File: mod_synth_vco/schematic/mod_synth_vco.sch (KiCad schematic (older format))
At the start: 15 parts

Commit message: Update schematic for vco
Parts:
- added C?: 10nf, symbol Device:C
- added C?: 1nf, symbol Device:C
- added J? (x3): AudioJack2, symbol Connector:AudioJack2
- added R? (x2): 100k, symbol Device:R
- added R? (x2): 10k, symbol Device:R
- added R?: 470k, symbol Device:R
- added RV? (x3): R_POT, symbol Device:R_POT
- added RV?: R_POT_TRIM, symbol Device:R_POT_TRIM
- added U? (x3): TL072, symbol Amplifier_Operational:TL072
- R?: value R -> 24k
- R?: value R -> 1m5
- R?: value R -> 5k6
- R? (x2): value R -> 100k
- R?: value R -> 620
- R?: value R -> 1k8
- R? (x2): value R -> 470
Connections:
- net +12V: now also R?.2, RV?.1, RV?.3, U?.8 (V+)
- net -12V: now also R?.2, U?.4 (V-)
- net GND: now also J?.S, R?.1, R?.2, U?.12 (GND), C?.2, C?.2, J?.S, J?.S, J?.S, R?.2, R?.2, RV?.3, RV?.3
- net at U?.1 (SCALE1): now also R?.1
- net at U?.11 (CAP): now also C?.1
- net at U?.13 (VLFI): now also R?.1, R?.1
- net at U?.14 (VS): now also R?.2
- net at U?.15 (VFCI): now also R?.1, R?.2, R?.2
- net at U?.2 (SCALE2): now also R?.1
- net at U?.3 (VEE): now also R?.1, R?.2, RV?.2, RV?.3
- net at U?.4 (VP): now also R?.1, R?.1, U?.3 (+)
- net at U?.5 (VPWM): now also R?.1
- net at R?.2: now also RV?.1
- net at R?.1: now also J?.T
- net at R?.2: now also C?.1
- net at R?.1: now also RV?.2
- new net: J?.T, RV?.1
- new net: R?.2, RV?.2 (x2)
- new net: J?.T, U?.1, U?.2 (-)
- new net: R?.1, R?.1, U?.5 (+)
- new net: R?.2, U?.6 (-), U?.7
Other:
- moved on the sheet: J?, R?, U?, U?A, U?B, U?C

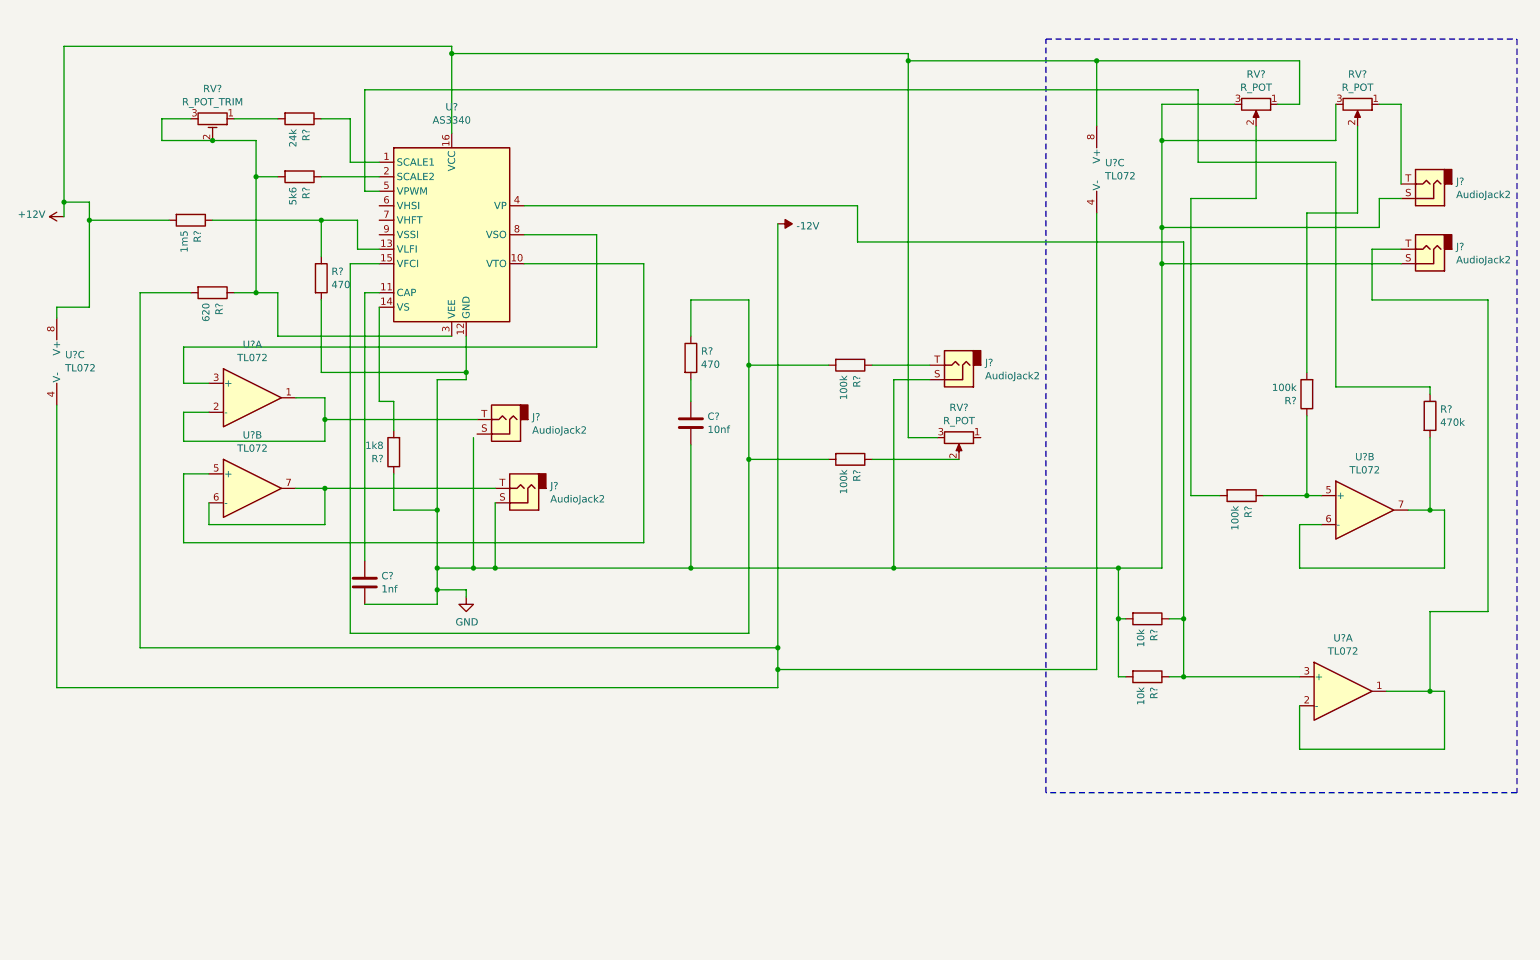
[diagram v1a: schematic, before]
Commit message: Add labels and cleanup square/PWM section
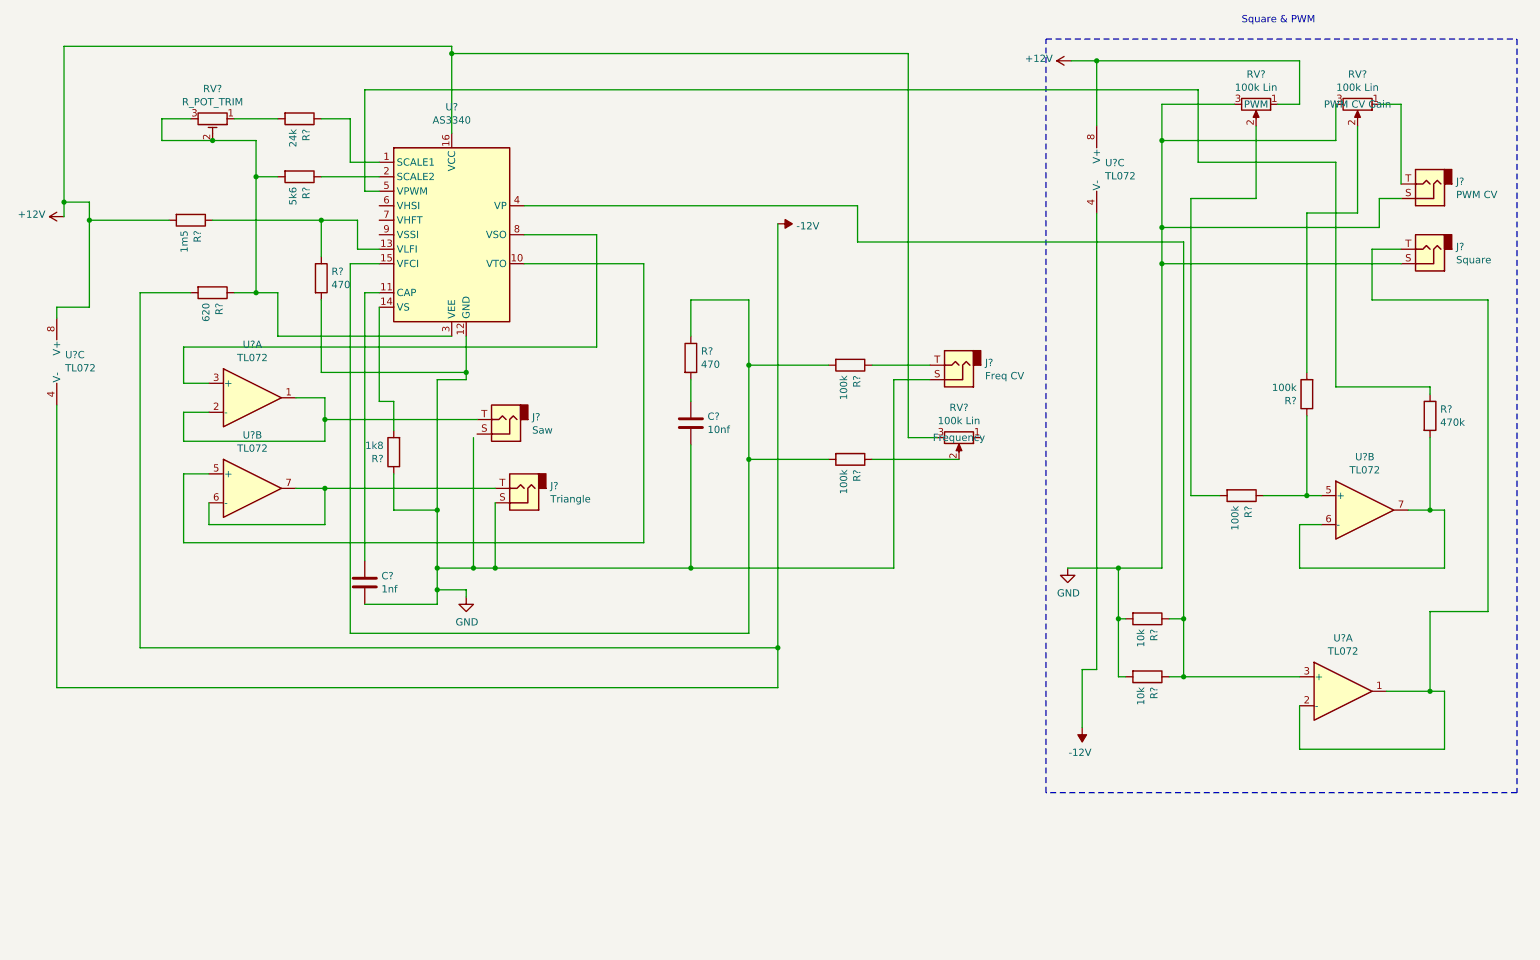
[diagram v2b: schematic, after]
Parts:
- J?: value AudioJack2 -> Freq CV
- J?: value AudioJack2 -> Saw
- J?: value AudioJack2 -> Triangle
- J?: value AudioJack2 -> PWM CV
- J?: value AudioJack2 -> Square
- RV?: value R_POT -> 100k Lin; Text (none) -> Frequency
- RV?: value R_POT -> 100k Lin; Text (none) -> PWM CV Gain
- RV?: value R_POT -> 100k Lin; Test (none) -> PWM
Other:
- note added: "Square & PWM"
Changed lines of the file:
@@
 P 4075 3375
 F 0 "J?" H 3895 3358 50  0000 R CNN
-F 1 "AudioJack2" H 3895 3449 50  0000 R CNN
+F 1 "Saw" H 3895 3449 50  0000 R CNN
 F 2 "" H 4075 3375 50  0001 C CNN
 F 3 "~" H 4075 3375 50  0001 C CNN
@@
 P 4200 3850
 F 0 "J?" H 4020 3833 50  0000 R CNN
-F 1 "AudioJack2" H 4020 3924 50  0000 R CNN
+F 1 "Triangle" H 4020 3924 50  0000 R CNN
 F 2 "" H 4200 3850 50  0001 C CNN
 F 3 "~" H 4200 3850 50  0001 C CNN
@@
 P 7200 3000
 F 0 "J?" H 7020 2983 50  0000 R CNN
-F 1 "AudioJack2" H 7020 3074 50  0000 R CNN
+F 1 "Freq CV" H 7020 3074 50  0000 R CNN
 F 2 "" H 7200 3000 50  0001 C CNN
 F 3 "~" H 7200 3000 50  0001 C CNN
@@
 P 7200 3500
 F 0 "RV?" V 6993 3500 50  0000 C CNN
-F 1 "R_POT" V 7084 3500 50  0000 C CNN
+F 1 "100k Lin" V 7084 3500 50  0000 C CNN
 F 2 "" H 7200 3500 50  0001 C CNN
 F 3 "~" H 7200 3500 50  0001 C CNN
+F 4 "Frequency" V 7200 3500 50  0000 C CNN "Text"
 	1    7200 3500
 	0    1    1    0
@@
 Connection ~ 5950 4950
 Wire Wire Line
-	5950 4950 5950 5100
-Wire Wire Line
 	3200 1700 2800 1700
 Wire Wire Line
@@
 Wire Wire Line
 	7050 3500 6850 3500
-Wire Wire Line
-	6850 3500 6850 900
 Wire Wire Line
 	6850 850  3700 850
@@
 P 9950 1200
 F 0 "RV?" V 9743 1200 50  0000 C CNN
-F 1 "R_POT" V 9834 1200 50  0000 C CNN
+F 1 "100k Lin" V 9834 1200 50  0000 C CNN
 F 2 "" H 9950 1200 50  0001 C CNN
 F 3 "~" H 9950 1200 50  0001 C CNN
+F 4 "PWM CV Gain" V 9950 1200 50  0000 C CNN "Text"
 	1    9950 1200
 	0    1    1    0
@@
 P 9250 1200
 F 0 "RV?" V 9043 1200 50  0000 C CNN
-F 1 "R_POT" V 9134 1200 50  0000 C CNN
+F 1 "100k Lin" V 9134 1200 50  0000 C CNN
 F 2 "" H 9250 1200 50  0001 C CNN
 F 3 "~" H 9250 1200 50  0001 C CNN
+F 4 "PWM" V 9250 1200 50  0000 C CNN "Test"
 	1    9250 1200
 	0    1    1    0
@@
 P 10450 1750
 F 0 "J?" H 10270 1733 50  0000 R CNN
-F 1 "AudioJack2" H 10270 1824 50  0000 R CNN
+F 1 "PWM CV" H 10270 1824 50  0000 R CNN
 F 2 "" H 10450 1750 50  0001 C CNN
 F 3 "~" H 10450 1750 50  0001 C CNN
@@
 P 10450 2200
 F 0 "J?" H 10270 2183 50  0000 R CNN
-F 1 "AudioJack2" H 10270 2274 50  0000 R CNN
+F 1 "Square" H 10270 2274 50  0000 R CNN
 F 2 "" H 10450 2200 50  0001 C CNN
 F 3 "~" H 10450 2200 50  0001 C CNN
@@
 	7800 750  11050 750
 Wire Wire Line
-	8150 900  6850 900
-Connection ~ 6850 900
-Wire Wire Line
-	6850 900  6850 850
+	8150 900  7975 900
 Wire Wire Line
 	8150 1350 8150 900
 Wire Wire Line
-	8150 5100 5950 5100
-Connection ~ 5950 5100
-Wire Wire Line
-	5950 5100 5950 5225
+	8150 5100 8050 5100
 Wire Wire Line
 	8150 900  9550 900
@@
 Wire Wire Line
 	6750 3100 6750 4400
-Connection ~ 6750 4400
-Wire Wire Line
-	6750 4400 8300 4400
 Wire Wire Line
 	2825 3850 4000 3850
@@
 Wire Wire Line
 	8600 2050 8600 2300
+$Comp
+L power:+12V #PWR?
+U 1 1 5D1CBB29
+P 7975 900
+F 0 "#PWR?" H 7975 750 50  0001 C CNN
+F 1 "+12V" V 7990 1028 50  0000 L CNN
+F 2 "" H 7975 900 50  0001 C CNN
+F 3 "" H 7975 900 50  0001 C CNN
+	1    7975 900
+	0    -1   -1   0
+$EndComp
+Wire Wire Line
+	6850 850  6850 3500
+$Comp
+L power:-12V #PWR?
+U 1 1 5D1CDC9F
+P 8050 5500
+F 0 "#PWR?" H 8050 5600 50  0001 C CNN
+F 1 "-12V" H 8065 5673 50  0000 C CNN
+F 2 "" H 8050 5500 50  0001 C CNN
+F 3 "" H 8050 5500 50  0001 C CNN
+	1    8050 5500
+	-1   0    0    1
+$EndComp
+$Comp
+L power:GND #PWR?
+U 1 1 5D1CE8BF
+P 7950 4400
+F 0 "#PWR?" H 7950 4150 50  0001 C CNN
+F 1 "GND" H 7955 4227 50  0000 C CNN
+F 2 "" H 7950 4400 50  0001 C CNN
+F 3 "" H 7950 4400 50  0001 C CNN
+	1    7950 4400
+	1    0    0    -1
+$EndComp
+Wire Wire Line
+	7950 4400 8300 4400
+Wire Wire Line
+	8050 5500 8050 5100
+Wire Wire Line
+	5950 4950 5950 5225
+Text Notes 9150 650  0    50   ~ 0
+Square & PWM
 $EndSCHEMATC

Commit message: Some PCB layout for VCO
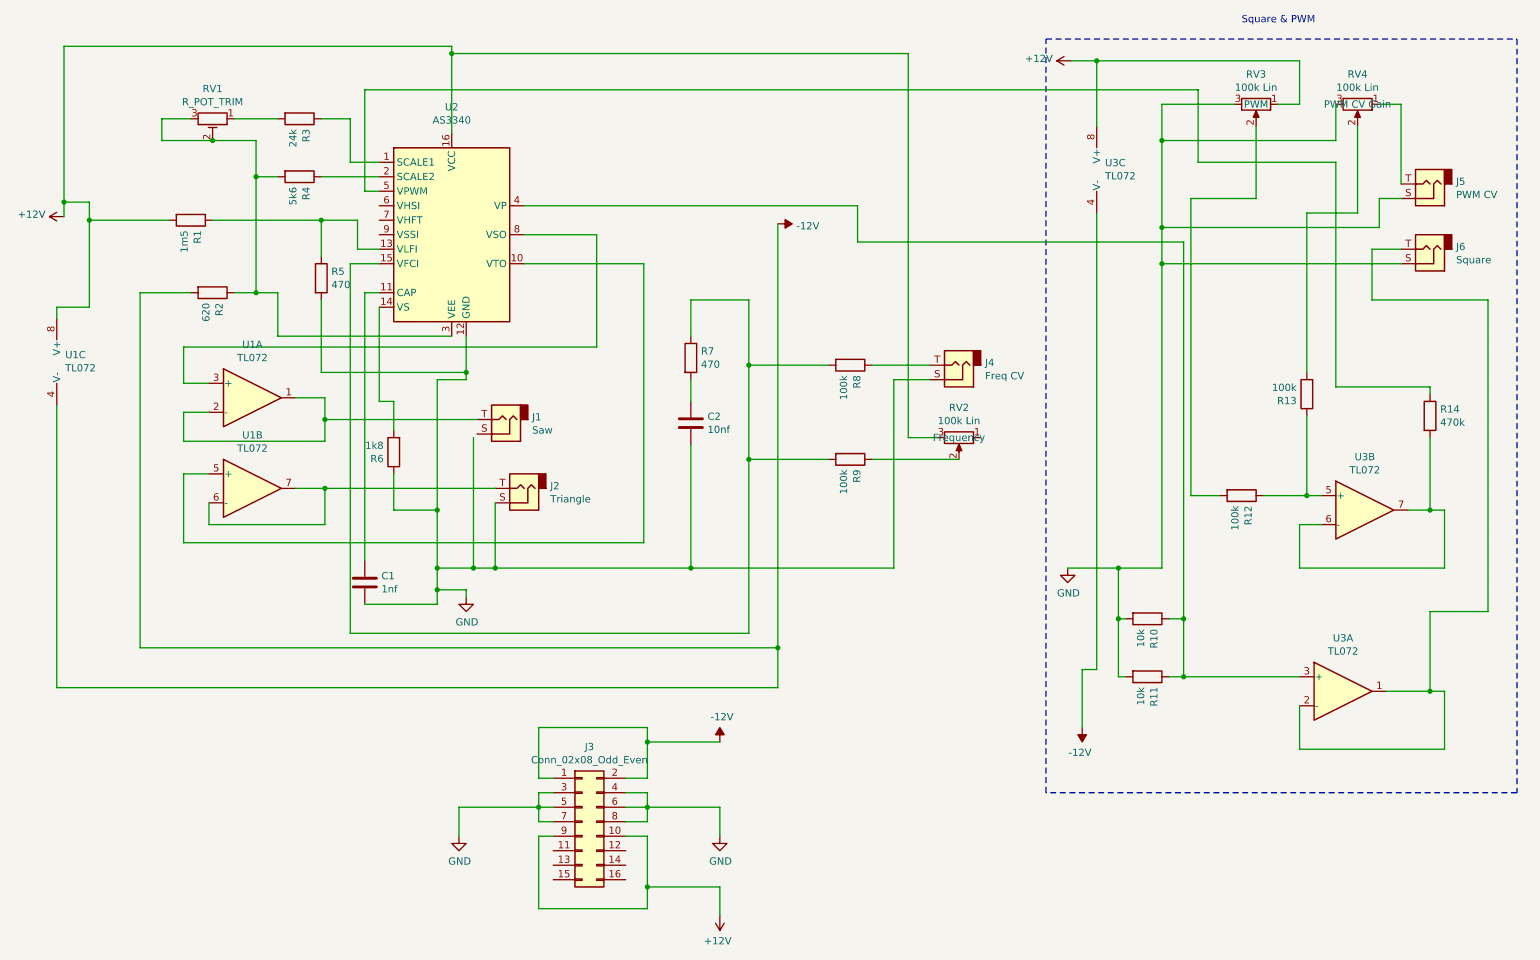
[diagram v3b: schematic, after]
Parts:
- added J3: Conn_02x08_Odd_Even, Connector_IDC:IDC-Header_2x08_P2.54mm_Vertical, symbol Connector_Generic:Conn_02x08_Odd_Even
- C1, C2: renamed from C?; footprint (none) -> Capacitor_THT:C_Disc_D9.0mm_W2.5mm_P5.00mm
- J1, J2, J4, J5, J6: renamed from J?; footprint (none) -> Connector_Audio:Jack_3.5mm_QingPu_WQP-PJ398SM_Vertical_CircularHoles
- R1, R10, R11, R12, R13, R14, R2, R3, R4, R5, R6, R7, R8, R9: renamed from R?; footprint (none) -> Resistor_THT:R_Axial_DIN0207_L6.3mm_D2.5mm_P10.16mm_Horizontal
- RV1: renamed from RV?; footprint (none) -> Potentiometer_THT:Potentiometer_Runtron_RM-065_Vertical
- RV2, RV3, RV4: renamed from RV?; footprint (none) -> Potentiometer_THT:Potentiometer_Alpha_RD901F-40-00D_Single_Vertical_CircularHoles
- U1, U3: renamed from U?; footprint (none) -> Package_DIP:DIP-8_W7.62mm_LongPads
- U2: renamed from U?; footprint (none) -> Package_DIP:DIP-16_W7.62mm_Socket_LongPads
- gave numbers to parts that had none: 2
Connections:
- net +12V: now also J3.10 (Pin_10), J3.9 (Pin_9)
- net -12V: now also J3.1 (Pin_1), J3.2 (Pin_2)
- net GND: now also J3.3 (Pin_3), J3.4 (Pin_4), J3.5 (Pin_5), J3.6 (Pin_6), J3.7 (Pin_7), J3.8 (Pin_8)

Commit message: Layout PCB
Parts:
- U1, U3: footprint Package_DIP:DIP-8_W7.62mm_LongPads -> Package_DIP:DIP-8_W7.62mm_Socket_LongPads

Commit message: Update schematic
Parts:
- RV1: value R_POT_TRIM -> 10k
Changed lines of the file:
@@
 P 2050 1300
 F 0 "RV1" V 1843 1300 50  0000 C CNN
-F 1 "R_POT_TRIM" V 1934 1300 50  0000 C CNN
+F 1 "10k" V 1934 1300 50  0000 C CNN
 F 2 "Potentiometer_THT:Potentiometer_Runtron_RM-065_Vertical" H 2050 1300 50  0001 C CNN
 F 3 "~" H 2050 1300 50  0001 C CNN

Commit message: Reverse pulse width knob and CV level
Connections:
- net +12V: now also RV3.3; no longer RV3.1
- net GND: now also RV3.1, RV4.1; no longer RV3.3, RV4.3
- net at J5.T: now also RV4.3; no longer RV4.1

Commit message: Connect J1 to GND
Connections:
- net GND: now also J1.S
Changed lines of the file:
@@
 	-1   0    0    1
 $EndComp
-Wire Wire Line
-	3850 3500 3850 4400
 $Comp
 L Device:R_POT RV3
@@
 Wire Wire Line
 	10250 900  10250 1750
+Wire Wire Line
+	3875 3475 3850 3475
+Wire Wire Line
+	3850 3475 3850 4400
 $EndSCHEMATC
